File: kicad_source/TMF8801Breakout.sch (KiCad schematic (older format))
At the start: 28 parts, among them CN1 CONN_01X06, CN2 CONN_01X07, CN3 SM05B-SRSS-TB, Q1 BSS138, Q2 BSS138, Q3 BSS138, U1 MIC5225-3.3, U2 TMF8801

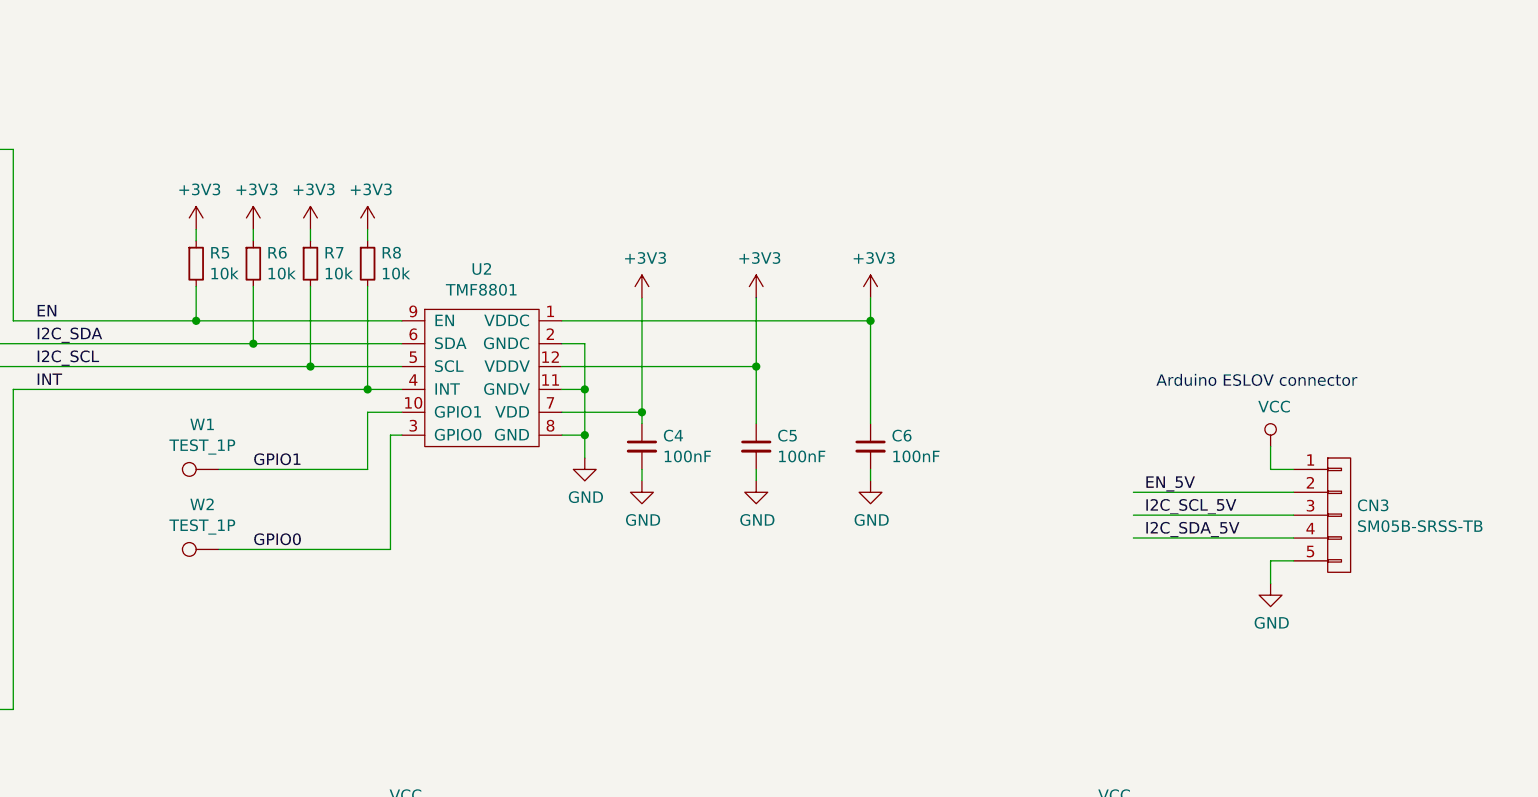
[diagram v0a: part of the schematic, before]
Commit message: added second ESLOV connector
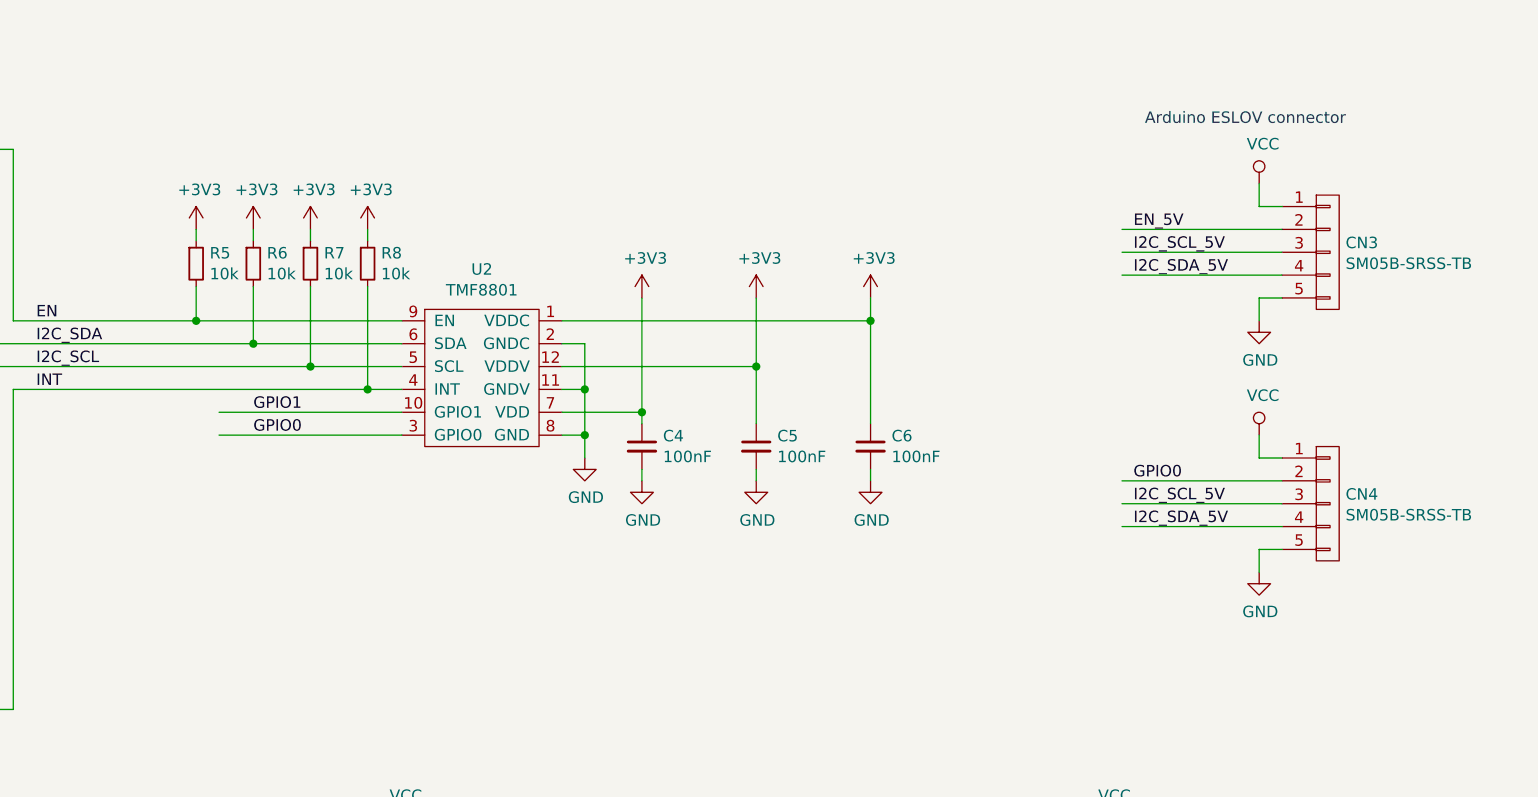
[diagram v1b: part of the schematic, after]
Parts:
- removed W1, W2: TEST_1P, wire_pads:SolderWirePad_single_1mmSMD, symbol mechanical-connectors:TEST_1P
- added CN4: SM05B-SRSS-TB, Connector_JST:JST_SH_SM05B-SRSS-TB_1x05-1MP_P1.00mm_Horizontal, symbol mechanical-connectors:CONN_01X05
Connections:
- wire segments 106 -> 109
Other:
- moved on the sheet: CN3
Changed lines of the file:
@@
 Sheet 1 1
 Title "TMF8801Breakout"
-Date "2020-11-25"
+Date "2020-11-27"
 Rev "0.1"
 Comp "genrationmake"
@@
 Wire Wire Line
 	5450 2300 5600 2300
-$Comp
-L mechanical-connectors:TEST_1P W1
-U 1 1 5FB7AFBE
-P 4800 2650
-F 0 "W1" V 4995 2722 50  0000 C CNN
-F 1 "TEST_1P" V 4904 2722 50  0000 C CNN
-F 2 "wire_pads:SolderWirePad_single_1mmSMD" H 5000 2650 50  0001 C CNN
-F 3 "" H 5000 2650 50  0000 C CNN
-	1    4800 2650
-	0    -1   -1   0
-$EndComp
-$Comp
-L mechanical-connectors:TEST_1P W2
-U 1 1 5FB7BF6B
-P 4800 3000
-F 0 "W2" V 4995 3072 50  0000 C CNN
-F 1 "TEST_1P" V 4904 3072 50  0000 C CNN
-F 2 "wire_pads:SolderWirePad_single_1mmSMD" H 5000 3000 50  0001 C CNN
-F 3 "" H 5000 3000 50  0000 C CNN
-	1    4800 3000
-	0    -1   -1   0
-$EndComp
-Wire Wire Line
-	4800 2650 5450 2650
-Wire Wire Line
-	5450 2650 5450 2400
-Wire Wire Line
-	5450 2400 5600 2400
-Wire Wire Line
-	4800 3000 5550 3000
-Wire Wire Line
-	5550 3000 5550 2500
-Wire Wire Line
-	5550 2500 5600 2500
-Text Label 4950 2650 0    50   ~ 0
+Text Label 4950 2400 0    50   ~ 0
 GPIO1
-Text Label 4950 3000 0    50   ~ 0
+Text Label 4950 2500 0    50   ~ 0
 GPIO0
 Wire Wire Line
@@
 L mechanical-connectors:CONN_01X05 CN3
 U 1 1 5FBEB318
-P 9700 2850
-F 0 "CN3" H 9778 2891 50  0000 L CNN
-F 1 "SM05B-SRSS-TB" H 9778 2800 50  0000 L CNN
-F 2 "Connector_JST:JST_SH_SM05B-SRSS-TB_1x05-1MP_P1.00mm_Horizontal" H 9700 2850 50  0001 C CNN
-F 3 "" H 9700 2850 50  0000 C CNN
-	1    9700 2850
+P 9650 1700
+F 0 "CN3" H 9728 1741 50  0000 L CNN
+F 1 "SM05B-SRSS-TB" H 9728 1650 50  0000 L CNN
+F 2 "Connector_JST:JST_SH_SM05B-SRSS-TB_1x05-1MP_P1.00mm_Horizontal" H 9650 1700 50  0001 C CNN
+F 3 "" H 9650 1700 50  0000 C CNN
+	1    9650 1700
 	1    0    0    -1
 $EndComp
@@
 L power-supply:VCC #PWR030
 U 1 1 5FBED847
-P 9400 2550
-F 0 "#PWR030" H 9400 2400 50  0001 C CNN
-F 1 "VCC" H 9417 2723 50  0000 C CNN
-F 2 "" H 9400 2550 50  0000 C CNN
-F 3 "" H 9400 2550 50  0000 C CNN
-	1    9400 2550
+P 9350 1400
+F 0 "#PWR030" H 9350 1250 50  0001 C CNN
+F 1 "VCC" H 9367 1573 50  0000 C CNN
+F 2 "" H 9350 1400 50  0000 C CNN
+F 3 "" H 9350 1400 50  0000 C CNN
+	1    9350 1400
 	1    0    0    -1
 $EndComp
@@
 L power-supply:GND #PWR031
 U 1 1 5FBEF9B4
-P 9400 3150
-F 0 "#PWR031" H 9400 2900 50  0001 C CNN
-F 1 "GND" H 9405 2977 50  0000 C CNN
-F 2 "" H 9400 3150 50  0000 C CNN
-F 3 "" H 9400 3150 50  0000 C CNN
-	1    9400 3150
-	1    0    0    -1
-$EndComp
-Wire Wire Line
-	9500 3050 9400 3050
-Wire Wire Line
-	9400 3050 9400 3150
-Wire Wire Line
-	8800 2950 9500 2950
-Wire Wire Line
-	8800 2850 9500 2850
-Wire Wire Line
-	8800 2750 9500 2750
-Wire Wire Line
-	9400 2550 9400 2650
-Wire Wire Line
-	9400 2650 9500 2650
-Text Label 8850 2950 0    50   ~ 0
+P 9350 2000
+F 0 "#PWR031" H 9350 1750 50  0001 C CNN
+F 1 "GND" H 9355 1827 50  0000 C CNN
+F 2 "" H 9350 2000 50  0000 C CNN
+F 3 "" H 9350 2000 50  0000 C CNN
+	1    9350 2000
+	1    0    0    -1
+$EndComp
+Wire Wire Line
+	9450 1900 9350 1900
+Wire Wire Line
+	9350 1900 9350 2000
+Wire Wire Line
+	8750 1800 9450 1800
+Wire Wire Line
+	8750 1700 9450 1700
+Wire Wire Line
+	8750 1600 9450 1600
+Wire Wire Line
+	9350 1400 9350 1500
+Wire Wire Line
+	9350 1500 9450 1500
+Text Label 8800 1800 0    50   ~ 0
 I2C_SDA_5V
-Text Label 8850 2850 0    50   ~ 0
+Text Label 8800 1700 0    50   ~ 0
 I2C_SCL_5V
-Text Label 8850 2750 0    50   ~ 0
+Text Label 8800 1600 0    50   ~ 0
 EN_5V
-Text Notes 8900 2300 0    50   ~ 0
+Text Notes 8850 1150 0    50   ~ 0
 Arduino ESLOV connector
+$Comp
+L mechanical-connectors:CONN_01X05 CN4
+U 1 1 5FC11B52
+P 9650 2800
+F 0 "CN4" H 9728 2841 50  0000 L CNN
+F 1 "SM05B-SRSS-TB" H 9728 2750 50  0000 L CNN
+F 2 "Connector_JST:JST_SH_SM05B-SRSS-TB_1x05-1MP_P1.00mm_Horizontal" H 9650 2800 50  0001 C CNN
+F 3 "" H 9650 2800 50  0000 C CNN
+	1    9650 2800
+	1    0    0    -1
+$EndComp
+$Comp
+L power-supply:VCC #PWR032
+U 1 1 5FC11D7A
+P 9350 2500
+F 0 "#PWR032" H 9350 2350 50  0001 C CNN
+F 1 "VCC" H 9367 2673 50  0000 C CNN
+F 2 "" H 9350 2500 50  0000 C CNN
+F 3 "" H 9350 2500 50  0000 C CNN
+	1    9350 2500
+	1    0    0    -1
+$EndComp
+$Comp
+L power-supply:GND #PWR033
+U 1 1 5FC11D84
+P 9350 3100
+F 0 "#PWR033" H 9350 2850 50  0001 C CNN
+F 1 "GND" H 9355 2927 50  0000 C CNN
+F 2 "" H 9350 3100 50  0000 C CNN
+F 3 "" H 9350 3100 50  0000 C CNN
+	1    9350 3100
+	1    0    0    -1
+$EndComp
+Wire Wire Line
+	9450 3000 9350 3000
+Wire Wire Line
+	9350 3000 9350 3100
+Wire Wire Line
+	8750 2900 9450 2900
+Wire Wire Line
+	8750 2800 9450 2800
+Wire Wire Line
+	8750 2700 9450 2700
+Wire Wire Line
+	9350 2500 9350 2600
+Wire Wire Line
+	9350 2600 9450 2600
+Text Label 8800 2900 0    50   ~ 0
+I2C_SDA_5V
+Text Label 8800 2800 0    50   ~ 0
+I2C_SCL_5V
+Text Label 8800 2700 0    50   ~ 0
+GPIO0
+Wire Wire Line
+	4800 2400 5600 2400
+Wire Wire Line
+	4800 2500 5600 2500
 $EndSCHEMATC
